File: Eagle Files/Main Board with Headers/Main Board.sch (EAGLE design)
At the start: 34 parts, among them Y1 16MHz

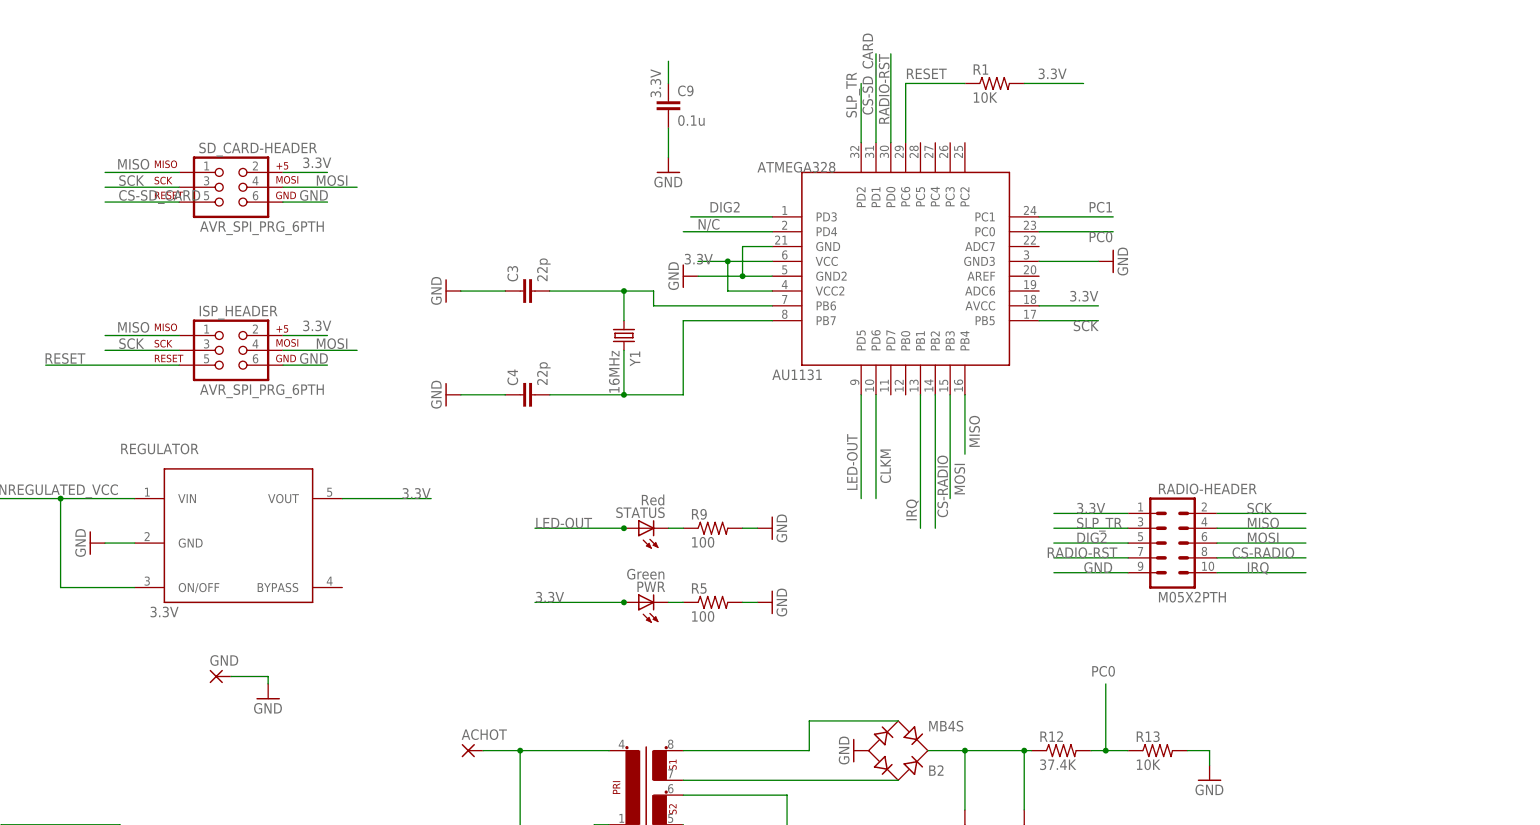
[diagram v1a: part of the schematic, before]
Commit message: Headers board now has the SD Card holder integrated into it.
This saves us board space, and brings us one step closer to a nice integrated board.

--Arthur

git-svn-id: http://cd-net.net/CPE496/trunk@115 05b6d0e0-c345-4a8e-a5b7-579c8bd0b646
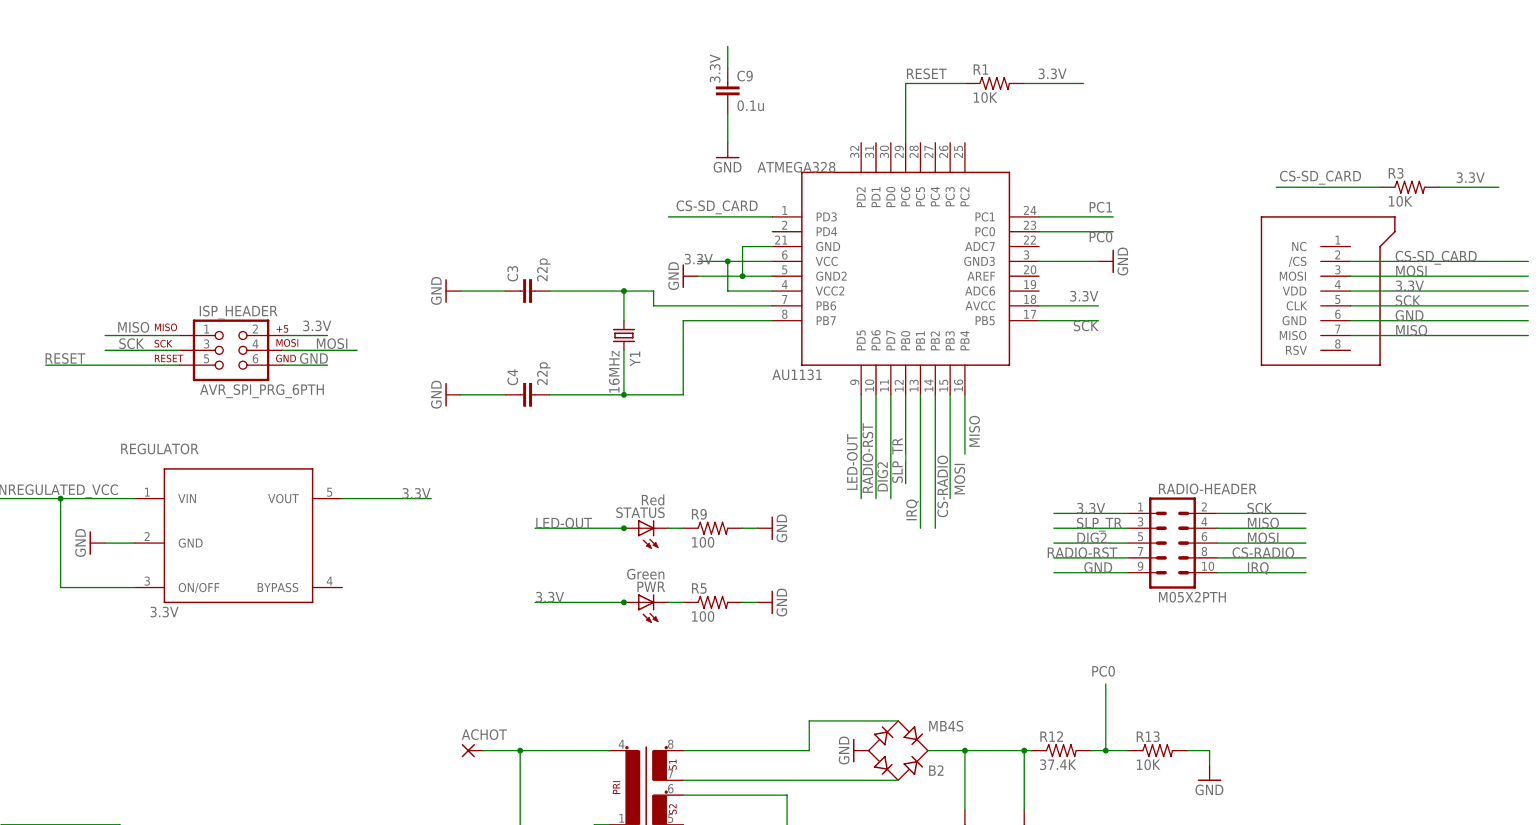
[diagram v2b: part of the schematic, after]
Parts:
- removed GND: (no value), wirepad:3,81/1,4
- removed SD_CARD-HEADER: AVR_SPI_PRG_6PTH, SparkFun:AVR_SPI_PRG_6PTH
- added R3: 10K, SparkFun:RESISTOR0603-RES
- added U$1: MICROSD, group10:MICROSD
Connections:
- removed net CLKM: U$2.PD6
- removed net N/C: U$2.PD4
- net 3.3V: now also R3.2, U$1.VDD; no longer SD_CARD-HEADER.2
- net CS-SD_CARD: now also R3.1, U$1./CS, U$2.PD3; no longer SD_CARD-HEADER.5, U$2.PD1
- net DIG2: now also U$2.PD7; no longer U$2.PD3
- net GND: now also U$1.GND; no longer GND.P, SD_CARD-HEADER.6
- net MISO: now also U$1.MISO; no longer SD_CARD-HEADER.1
- net MOSI: now also U$1.MOSI; no longer SD_CARD-HEADER.4
- net RADIO-RST: now also U$2.PD6; no longer U$2.PD0
- net SCK: now also U$1.CLK; no longer SD_CARD-HEADER.3
- net SLP_TR: now also U$2.PB0; no longer U$2.PD2
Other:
- moved on the sheet: C9
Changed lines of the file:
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@@
 <setting verticaltext="up"/>
 </settings>
-<grid distance="0.05" unitdist="inch" unit="inch" style="lines" multiple="1" display="yes" altdistance="0.005" altunitdist="inch" altunit="inch"/>
+<grid distance="0.1" unitdist="inch" unit="inch" style="lines" multiple="1" display="no" altdistance="0.01" altunitdist="inch" altunit="inch"/>
 <layers>
 <layer number="1" name="Top" color="4" fill="1" visible="no" active="no"/>
@@
 <class number="0" name="default" width="0" drill="0">
 </class>
-<class number="1" name="Mini" width="0.25" drill="0">
-</class>
 </classes>
 <parts>
@@
 <part name="C3" library="SparkFun" deviceset="CAP" device="0603-CAP" value="22p"/>
 <part name="C4" library="SparkFun" deviceset="CAP" device="0603-CAP" value="22p"/>
-<part name="GND11" library="supply1" deviceset="GND" device=""/>
 <part name="C1" library="SparkFun" deviceset="CAP" device="0603-CAP" value="0.1u"/>
 <part name="GND12" library="supply1" deviceset="GND" device=""/>
@@
 <part name="ACHOT" library="wirepad" deviceset="3,81/1,4" device=""/>
 <part name="ACNEU" library="wirepad" deviceset="3,81/1,4" device=""/>
-<part name="GND" library="wirepad" deviceset="3,81/1,4" device=""/>
 <part name="ACOUT" library="wirepad" deviceset="3,81/1,4" device=""/>
 <part name="ISP_HEADER" library="SparkFun" deviceset="AVR_SPI_PRG_6" device="PTH"/>
@@
 <part name="JP4" library="SparkFun" deviceset="STAND-OFF" device=""/>
 <part name="RADIO-HEADER" library="SparkFun" deviceset="M05X2" device="PTH"/>
-<part name="SD_CARD-HEADER" library="SparkFun" deviceset="AVR_SPI_PRG_6" device="PTH"/>
+<part name="U$1" library="group10" deviceset="MICROSD" device=""/>
+<part name="R3" library="SparkFun" deviceset="RESISTOR" device="0603-RES" value="10K"/>
 </parts>
 <sheets>
@@
 <instance part="C3" gate="G$1" x="-66.04" y="76.2" rot="R90"/>
 <instance part="C4" gate="G$1" x="-66.04" y="58.42" rot="R90"/>
-<instance part="GND11" gate="1" x="-111.76" y="6.35"/>
 <instance part="C1" gate="G$1" x="-139.7" y="-38.1" rot="R180"/>
 <instance part="GND12" gate="1" x="-139.7" y="-48.26"/>
@@
 <instance part="ACHOT" gate="1" x="-77.47" y="-2.54"/>
 <instance part="ACNEU" gate="1" x="-48.26" y="-24.13" rot="R180"/>
-<instance part="GND" gate="1" x="-120.65" y="10.16"/>
 <instance part="ACOUT" gate="1" x="-93.98" y="-22.86" rot="R180"/>
 <instance part="ISP_HEADER" gate="G$1" x="-119.38" y="66.04"/>
@@
 <instance part="GND4" gate="1" x="17.78" y="-25.4"/>
 <instance part="GND15" gate="1" x="7.62" y="-25.4"/>
-<instance part="C9" gate="G$1" x="-43.18" y="106.68"/>
-<instance part="GND17" gate="1" x="-43.18" y="96.52"/>
+<instance part="C9" gate="G$1" x="-33.02" y="109.22"/>
+<instance part="GND17" gate="1" x="-33.02" y="99.06"/>
 <instance part="PWR" gate="G$1" x="-48.26" y="22.86" rot="R90"/>
 <instance part="R5" gate="G$1" x="-35.56" y="22.86"/>
@@
 <instance part="JP4" gate="G$1" x="-113.03" y="-50.8"/>
 <instance part="RADIO-HEADER" gate="G$1" x="43.18" y="33.02"/>
-<instance part="SD_CARD-HEADER" gate="G$1" x="-119.38" y="93.98"/>
+<instance part="U$1" gate="G$1" x="66.04" y="76.2" rot="R270"/>
+<instance part="R3" gate="G$1" x="83.82" y="93.98"/>
 </instances>
 <busses>
@@
 </segment>
 <segment>
-<pinref part="GND" gate="1" pin="P"/>
-<wire x1="-111.76" y1="10.16" x2="-118.11" y2="10.16" width="0.1524" layer="91"/>
-<pinref part="GND11" gate="1" pin="GND"/>
-<wire x1="-111.76" y1="8.89" x2="-111.76" y2="10.16" width="0.1524" layer="91"/>
-</segment>
-<segment>
 <pinref part="GND17" gate="1" pin="GND"/>
 <pinref part="C9" gate="G$1" pin="2"/>
-<wire x1="-43.18" y1="99.06" x2="-43.18" y2="104.14" width="0.1524" layer="91"/>
+<wire x1="-33.02" y1="101.6" x2="-33.02" y2="106.68" width="0.1524" layer="91"/>
 </segment>
 <segment>
@@
 </segment>
 <segment>
-<pinref part="SD_CARD-HEADER" gate="G$1" pin="6"/>
-<wire x1="-109.22" y1="91.44" x2="-101.6" y2="91.44" width="0.1524" layer="91"/>
-<label x="-106.426" y="91.694" size="1.778" layer="95"/>
+<pinref part="U$1" gate="G$1" pin="GND"/>
+<wire x1="73.66" y1="71.12" x2="104.14" y2="71.12" width="0.1524" layer="91"/>
+<label x="81.28" y="71.12" size="1.778" layer="95"/>
 </segment>
 </net>
@@
 </segment>
 <segment>
-<pinref part="SD_CARD-HEADER" gate="G$1" pin="4"/>
-<wire x1="-109.22" y1="93.98" x2="-96.52" y2="93.98" width="0.1524" layer="91"/>
-<label x="-103.632" y="94.234" size="1.778" layer="95"/>
+<pinref part="U$1" gate="G$1" pin="MOSI"/>
+<wire x1="73.66" y1="78.74" x2="104.14" y2="78.74" width="0.1524" layer="91"/>
+<label x="81.28" y="78.74" size="1.778" layer="95"/>
 </segment>
 </net>
@@
 <segment>
 <pinref part="C9" gate="G$1" pin="1"/>
-<wire x1="-43.18" y1="111.76" x2="-43.18" y2="115.57" width="0.1524" layer="91"/>
-<label x="-44.45" y="109.22" size="1.778" layer="95" rot="R90"/>
+<wire x1="-33.02" y1="114.3" x2="-33.02" y2="118.11" width="0.1524" layer="91"/>
+<label x="-34.29" y="111.76" size="1.778" layer="95" rot="R90"/>
 </segment>
 <segment>
@@
 </segment>
 <segment>
-<pinref part="SD_CARD-HEADER" gate="G$1" pin="2"/>
-<wire x1="-109.22" y1="96.52" x2="-101.6" y2="96.52" width="0.1524" layer="91"/>
-<label x="-105.918" y="97.282" size="1.778" layer="95"/>
+<pinref part="U$1" gate="G$1" pin="VDD"/>
+<wire x1="73.66" y1="76.2" x2="104.14" y2="76.2" width="0.1524" layer="91"/>
+<label x="81.28" y="76.2" size="1.778" layer="95"/>
+</segment>
+<segment>
+<pinref part="R3" gate="G$1" pin="2"/>
+<wire x1="88.9" y1="93.98" x2="99.06" y2="93.98" width="0.1524" layer="91"/>
+<label x="91.694" y="94.742" size="1.778" layer="95"/>
 </segment>
 </net>
@@
 </segment>
 <segment>
-<pinref part="SD_CARD-HEADER" gate="G$1" pin="3"/>
-<wire x1="-127" y1="93.98" x2="-139.7" y2="93.98" width="0.1524" layer="91"/>
-<label x="-137.414" y="94.234" size="1.778" layer="95"/>
+<pinref part="U$1" gate="G$1" pin="CLK"/>
+<wire x1="73.66" y1="73.66" x2="104.14" y2="73.66" width="0.1524" layer="91"/>
+<label x="81.28" y="73.66" size="1.778" layer="95"/>
 </segment>
 </net>
 <net name="CS-SD_CARD" class="0">
 <segment>
-<pinref part="U$2" gate="G$1" pin="PD1"/>
-<wire x1="-7.62" y1="101.6" x2="-7.62" y2="116.84" width="0.1524" layer="91"/>
-<label x="-8.128" y="106.299" size="1.778" layer="95" rot="R90"/>
-</segment>
-<segment>
-<pinref part="SD_CARD-HEADER" gate="G$1" pin="5"/>
-<wire x1="-127" y1="91.44" x2="-139.7" y2="91.44" width="0.1524" layer="91"/>
-<label x="-137.414" y="91.694" size="1.778" layer="95"/>
+<pinref part="U$1" gate="G$1" pin="/CS"/>
+<wire x1="73.66" y1="81.28" x2="104.14" y2="81.28" width="0.1524" layer="91"/>
+<label x="81.28" y="81.28" size="1.778" layer="95"/>
+</segment>
+<segment>
+<pinref part="R3" gate="G$1" pin="1"/>
+<wire x1="78.74" y1="93.98" x2="60.96" y2="93.98" width="0.1524" layer="91"/>
+<label x="61.468" y="94.996" size="1.778" layer="95"/>
+</segment>
+<segment>
+<pinref part="U$2" gate="G$1" pin="PD3"/>
+<wire x1="-25.4" y1="88.9" x2="-43.18" y2="88.9" width="0.1524" layer="91"/>
+<label x="-41.91" y="89.916" size="1.778" layer="95"/>
 </segment>
 </net>
@@
 </segment>
 <segment>
-<pinref part="SD_CARD-HEADER" gate="G$1" pin="1"/>
-<wire x1="-127" y1="96.52" x2="-139.7" y2="96.52" width="0.1524" layer="91"/>
-<label x="-137.668" y="97.028" size="1.778" layer="95"/>
+<pinref part="U$1" gate="G$1" pin="MISO"/>
+<wire x1="73.66" y1="68.58" x2="104.14" y2="68.58" width="0.1524" layer="91"/>
+<label x="81.28" y="68.58" size="1.778" layer="95"/>
 </segment>
 </net>
@@
 <net name="RADIO-RST" class="0">
 <segment>
-<pinref part="U$2" gate="G$1" pin="PD0"/>
-<wire x1="-5.08" y1="101.6" x2="-5.08" y2="116.84" width="0.1524" layer="91"/>
-<label x="-5.334" y="104.648" size="1.778" layer="95" rot="R90"/>
-</segment>
-<segment>
 <pinref part="RADIO-HEADER" gate="G$1" pin="7"/>
 <wire x1="35.56" y1="30.48" x2="22.86" y2="30.48" width="0.1524" layer="91"/>
 <label x="21.59" y="30.48" size="1.778" layer="95"/>
 </segment>
+<segment>
+<pinref part="U$2" gate="G$1" pin="PD6"/>
+<wire x1="-7.62" y1="58.42" x2="-7.62" y2="40.64" width="0.1524" layer="91"/>
+<label x="-8.128" y="41.402" size="1.778" layer="95" rot="R90"/>
+</segment>
 </net>
 <net name="SLP_TR" class="0">
-<segment>
-<pinref part="U$2" gate="G$1" pin="PD2"/>
-<wire x1="-10.16" y1="101.6" x2="-10.16" y2="111.76" width="0.1524" layer="91"/>
-<label x="-10.922" y="105.791" size="1.778" layer="95" rot="R90"/>
-</segment>
 <segment>
 <pinref part="RADIO-HEADER" gate="G$1" pin="3"/>
@@
 <label x="26.67" y="35.56" size="1.778" layer="95"/>
 </segment>
+<segment>
+<pinref part="U$2" gate="G$1" pin="PB0"/>
+<wire x1="-2.54" y1="58.42" x2="-2.54" y2="43.18" width="0.1524" layer="91"/>
+<label x="-3.048" y="43.18" size="1.778" layer="95" rot="R90"/>
+</segment>
 </net>
 <net name="IRQ" class="0">
@@
 <net name="DIG2" class="0">
 <segment>
-<pinref part="U$2" gate="G$1" pin="PD3"/>
-<wire x1="-25.4" y1="88.9" x2="-39.37" y2="88.9" width="0.1524" layer="91"/>
-<label x="-36.195" y="89.662" size="1.778" layer="95"/>
-</segment>
-<segment>
 <pinref part="RADIO-HEADER" gate="G$1" pin="5"/>
 <wire x1="35.56" y1="33.02" x2="22.86" y2="33.02" width="0.1524" layer="91"/>
 <label x="26.67" y="33.02" size="1.778" layer="95"/>
+</segment>
+<segment>
+<pinref part="U$2" gate="G$1" pin="PD7"/>
+<wire x1="-5.08" y1="58.42" x2="-5.08" y2="40.64" width="0.1524" layer="91"/>
+<label x="-5.588" y="41.656" size="1.778" layer="95" rot="R90"/>
 </segment>
 </net>
@@
 </segment>
 </net>
-<net name="CLKM" class="0">
-<segment>
-<pinref part="U$2" gate="G$1" pin="PD6"/>
-<wire x1="-7.62" y1="58.42" x2="-7.62" y2="40.64" width="0.1524" layer="91"/>
-<label x="-5.08" y="43.18" size="1.778" layer="95" rot="R90"/>
-</segment>
-</net>
-<net name="N/C" class="0">
-<segment>
-<pinref part="U$2" gate="G$1" pin="PD4"/>
-<wire x1="-25.4" y1="86.36" x2="-40.64" y2="86.36" width="0.1524" layer="91"/>
-<label x="-38.227" y="86.741" size="1.778" layer="95"/>
-</segment>
-</net>
